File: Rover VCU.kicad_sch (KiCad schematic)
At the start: 6 parts, among them J3 430450400, J6 430451200

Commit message: feat: implmeneted revamp with normal ethernet LAN8742A
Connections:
- net TRD_N: no longer names the net of J6.1 (Pin_1)
- net TRD_P: no longer names the net of J6.7 (Pin_7)
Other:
- sheet PHY ports: added none; removed TRD_N, TRD_P
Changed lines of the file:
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@@
 	(wire
 		(pts
-			(xy 69.85 93.98) (xy 92.71 93.98)
-		)
-		(stroke
-			(width 0)
-			(type default)
-		)
-	)
-	(wire
-		(pts
 			(xy 77.47 55.88) (xy 86.36 55.88)
 		)
@@
 	(wire
 		(pts
-			(xy 69.85 96.52) (xy 92.71 96.52)
-		)
-		(stroke
-			(width 0)
-			(type default)
-		)
-	)
-	(wire
-		(pts
 			(xy 118.11 101.6) (xy 134.62 101.6)
 		)
@@
 		)
 	)
-	(label "TRD_N"
-		(at 240.03 91.44 180)
-		(effects
-			(font
-				(size 1.27 1.27)
-			)
-			(justify right bottom)
-		)
-	)
-	(label "TRD_P"
-		(at 252.73 91.44 0)
-		(effects
-			(font
-				(size 1.27 1.27)
-			)
-			(justify left bottom)
-		)
-	)
 	(label "CAN1_N"
 		(at 240.03 101.6 180)
@@
 		)
 	)
-	(label "TRD_P"
-		(at 69.85 96.52 0)
-		(effects
-			(font
-				(size 1.27 1.27)
-			)
-			(justify left bottom)
-		)
-	)
 	(label "ESTOP"
 		(at 171.45 81.28 180)
@@
 		)
 	)
-	(label "TRD_N"
-		(at 69.85 93.98 0)
-		(effects
-			(font
-				(size 1.27 1.27)
-			)
-			(justify left bottom)
-		)
-	)
 	(symbol
 		(lib_id "power:GND")
@@
 			(effects
 				(font
-					(size 1.27 1.27)
-				)
-				(justify left)
-			)
-		)
-		(pin "TRD_N" input
-			(at 92.71 93.98 180)
-			(effects
-				(font
-					(size 1.27 1.27)
-				)
-				(justify left)
-			)
-		)
-		(pin "TRD_P" input
-			(at 92.71 96.52 180)
-			(effects
-				(font

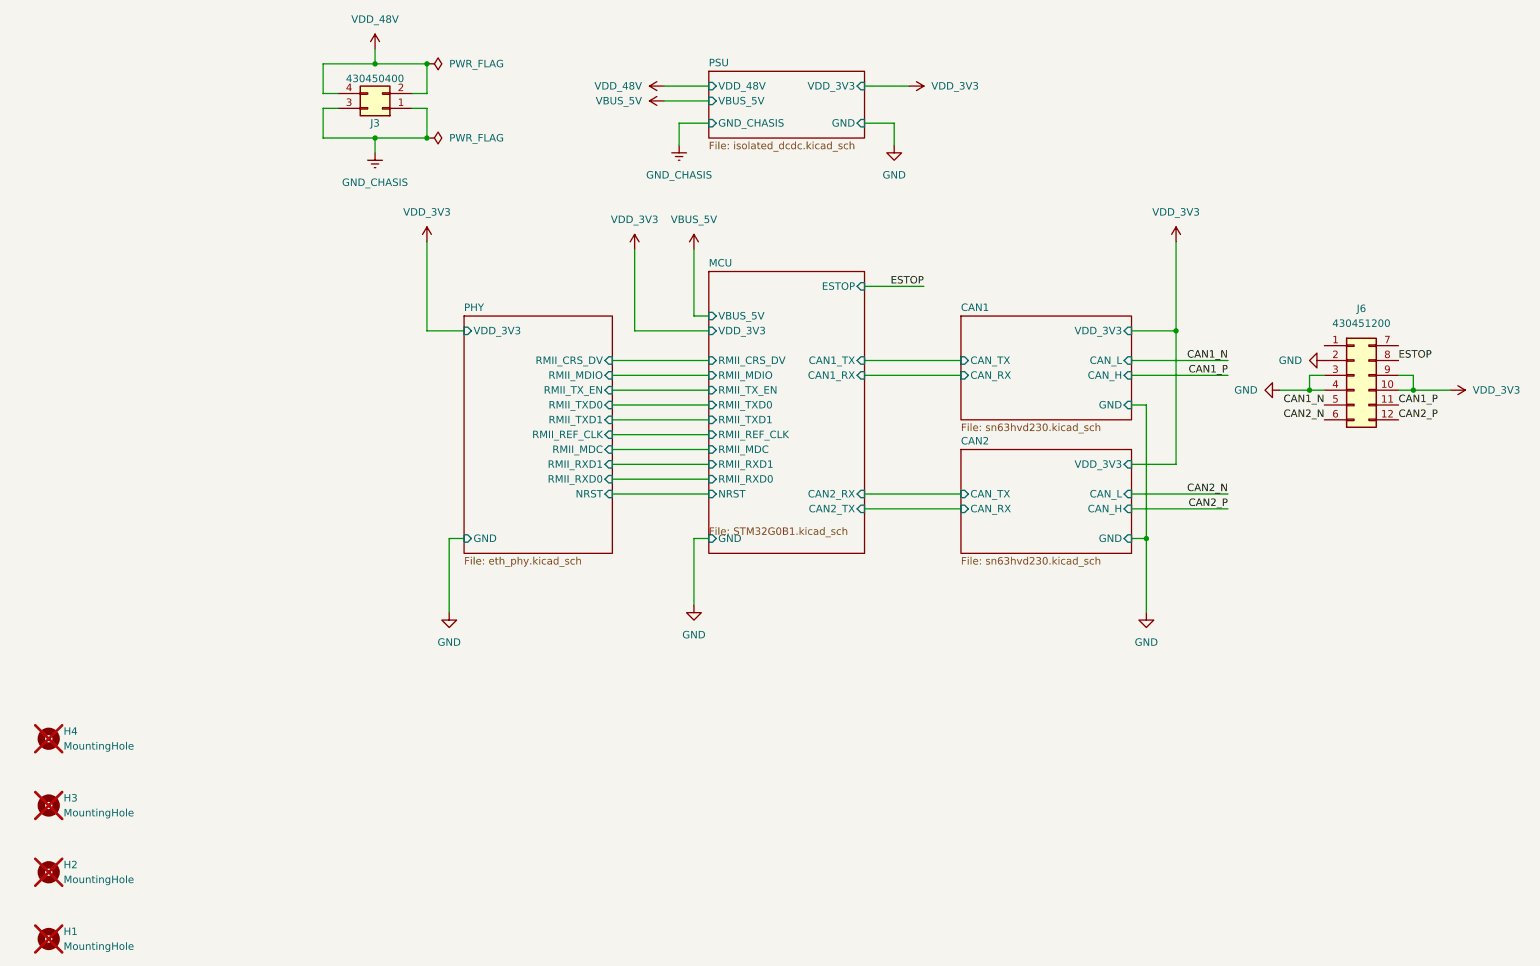
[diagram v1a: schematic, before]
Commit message: fix(eth_phy): completed revamp with lan8742a
BREAKING CHANGE:
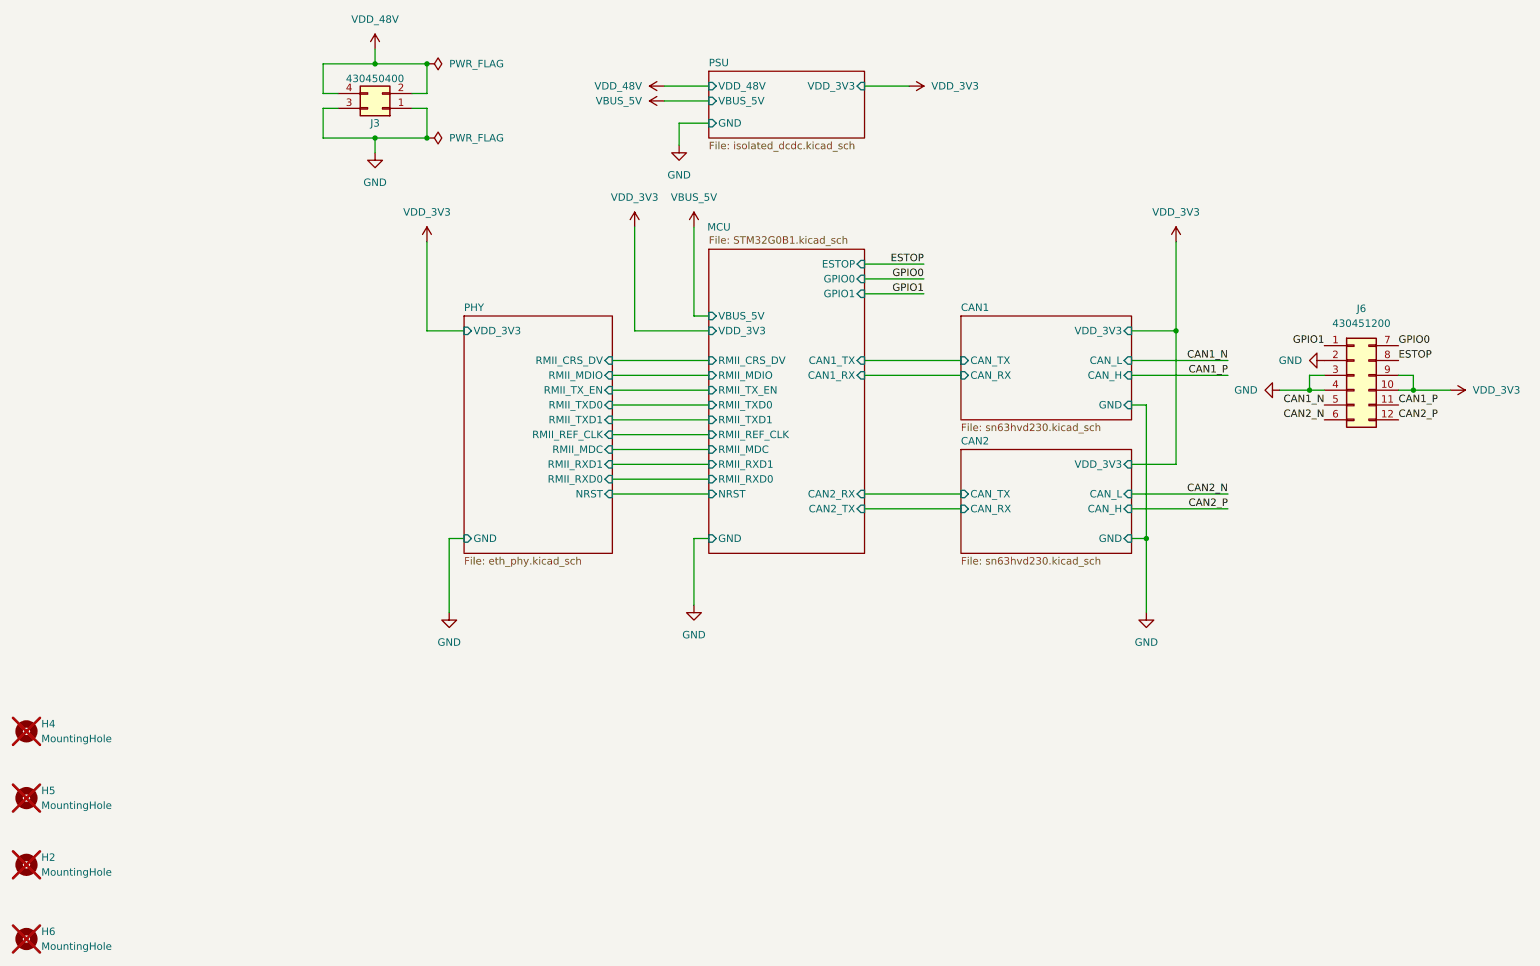
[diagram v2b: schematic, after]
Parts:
- removed H1, H3: MountingHole, symbol Mechanical:MountingHole
- added H5, H6: MountingHole, MountingHole:MountingHole_3.2mm_M3, symbol Mechanical:MountingHole
- H2, H4: footprint (none) -> MountingHole:MountingHole_3.2mm_M3
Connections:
- net GND_CHASIS is gone; now on net GND: J3.1 (Pin_1), J3.3 (Pin_3)
- net GPIO1: now reaches J6.1 (Pin_1)
- net GPIO0: now reaches J6.7 (Pin_7)
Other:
- sheet MCU ports: added GPIO0, GPIO1; removed none
- sheet PSU ports: added none; removed GND_CHASIS
- moved on the sheet: H2, H4
